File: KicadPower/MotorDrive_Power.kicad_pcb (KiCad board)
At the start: 6 copper layers, 91 x 71 mm, 347 parts, among them P1 PIN 2, P2 PIN 2, P3 PIN 2, P4 Connector, P5 Connector, P6 Header 20X2, P7 Connector, P8 Connector, P9 Connector, Q1 IGB110S101, Q10 IGB110S101, Q11 IGB110S101, Q12 IGB110S101, Q13 IGB110S101, Q14 IGB110S101, Q15 IGB110S101, Q16 IGB110S101, Q17 IGB110S101, Q18 IGB110S101, Q19 IGB110S101, Q2 IGB110S101, Q20 IGB110S101, Q21 IGB110S101, Q22 IGB110S101, Q23 IGB110S101, Q24 IGB110S101, Q3 IGB110S101, Q4 IGB110S101, Q5 IGB110S101, Q6 IGB110S101, Q7 IGB110S101, Q8 IGB110S101, Q9 IGB110S101, U1 TLE4972-AE35S5, U10 LDK220C-R, U11 1EDN7116UXTSA1, U12 1EDN7116UXTSA1, U13 1EDN7116UXTSA1, U14 1EDN7116UXTSA1, U15 1EDN7116UXTSA1, U16 1EDN7116UXTSA1, U17 TMP1075DGKR, U18 TMP1075DGKR, U19 TMP1075DGKR, U2 TLE4972-AE35S5, U3 TLE4972-AE35S5, U4 LDK220C-R, U5 LDK220C, U6 LDK220C, U7 LDK220C, U8 LDK220C-R, U9 LDK220C-R

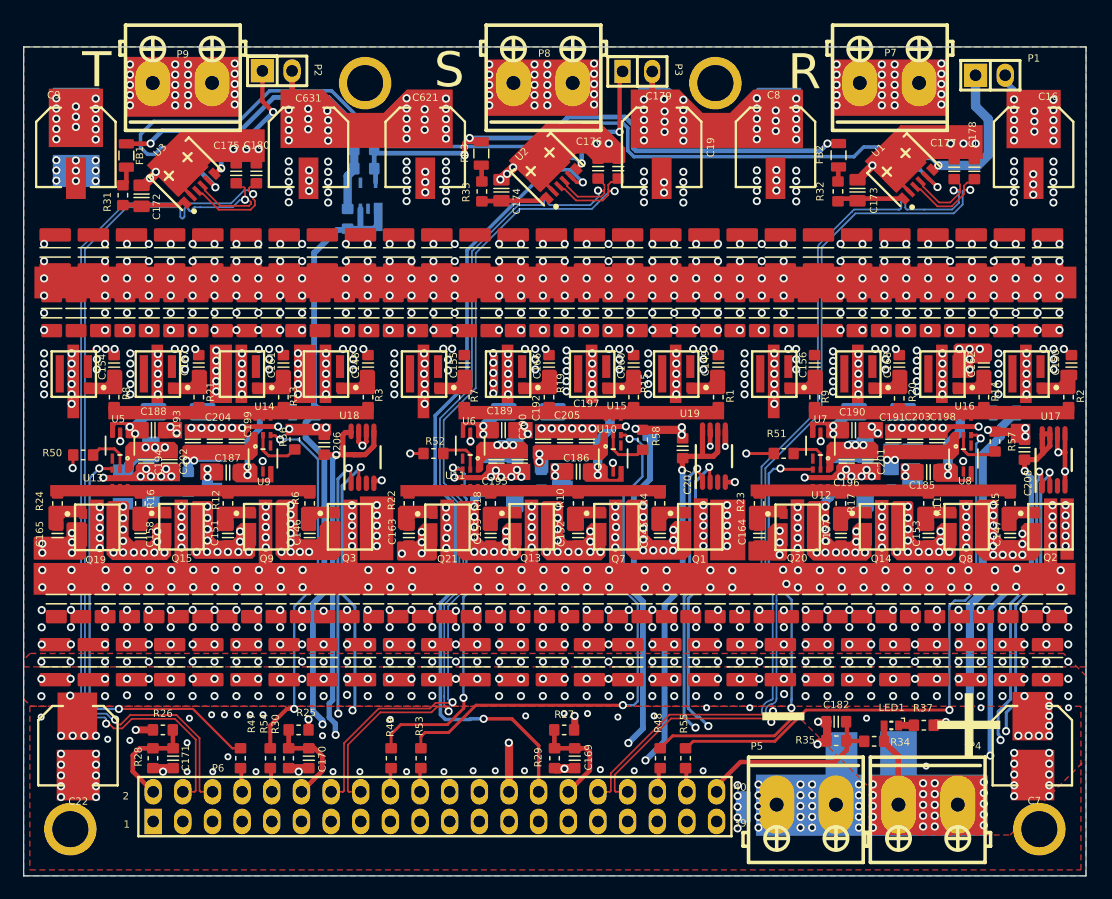
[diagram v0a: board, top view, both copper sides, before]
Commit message: new G serie of Driver modifed and finished
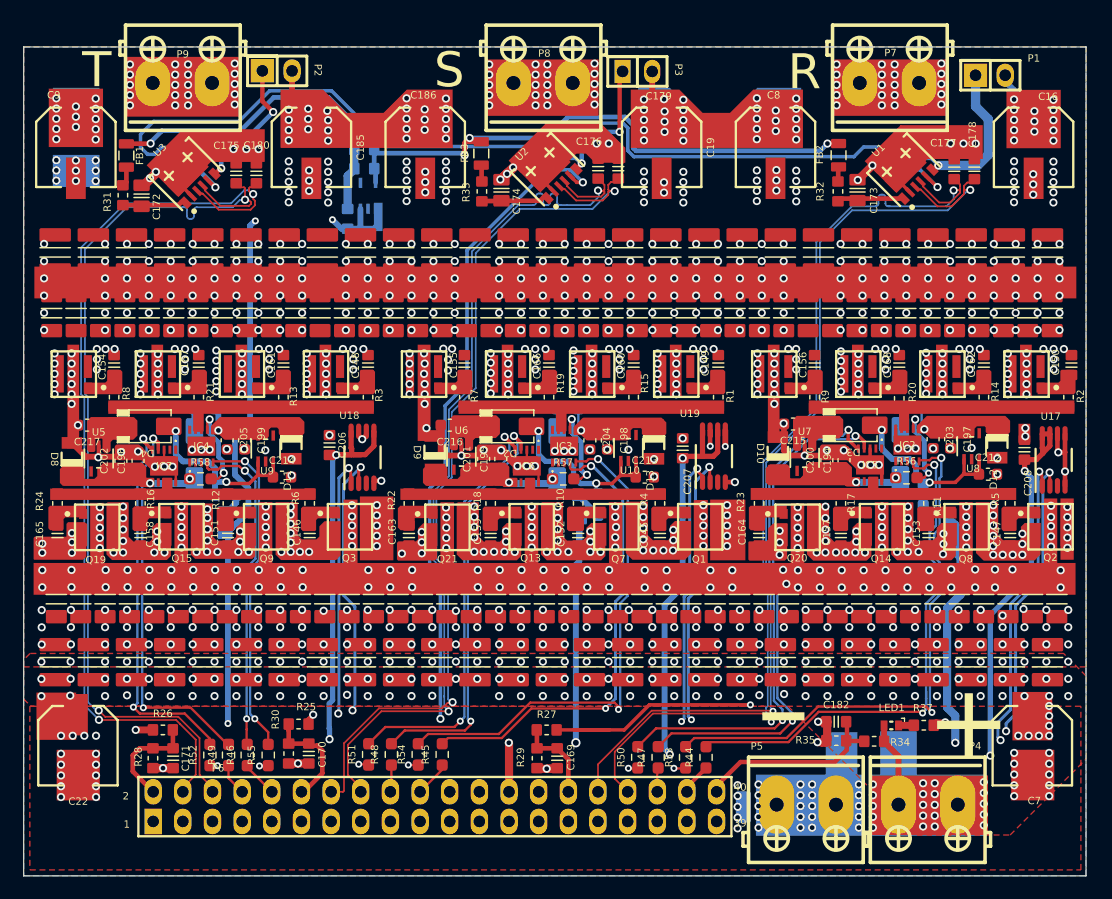
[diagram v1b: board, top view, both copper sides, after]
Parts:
- removed ? (x4): , 
- removed C187, C188, C189, C190, C191, C192, C193: Cap SMD, RezaLIB:CAPC2012X135N
- removed C621, C631: Cap Pol, RezaLIB:CAP-6.3-7.7
- removed R38, R39, R40: Res SMD, RezaLIB:RESC1608X55N
- removed U11, U12, U13, U14, U15, U16: 1EDN7116UXTSA1, RezaLIB:PG-TSNP-7-11_INF
- added C212: 10uF, Capacitor_SMD:C_0603_1608Metric, F.Cu at (185.6, 106.1)
- added C213: 10uF, Capacitor_SMD:C_0603_1608Metric, F.Cu at (156.2, 106.4)
- added C214: 10uF, Capacitor_SMD:C_0603_1608Metric, F.Cu at (125.1, 106.4)
- added C215: 10uF, Capacitor_SMD:C_0603_1608Metric, F.Cu at (168.9, 101.8)
- added C216: 10uF, Capacitor_SMD:C_0603_1608Metric, F.Cu at (139.5, 101.9)
- added C217: 10uF, Capacitor_SMD:C_0603_1608Metric, F.Cu at (108.4, 101.9)
- added IC2: 1EDN7116GXTMA1, 1EDN7116GXTMA1:1EDN7116GXTMA1, F.Cu at (178.7, 103.6)
- added IC3: 1EDN7116GXTMA1, 1EDN7116GXTMA1:1EDN7116GXTMA1, F.Cu at (149.3, 103.7)
- added IC4: 1EDN7116GXTMA1, 1EDN7116GXTMA1:1EDN7116GXTMA1, F.Cu at (118.2, 103.7)
- added IC5: 1EDN7116GXTMA1, 1EDN7116GXTMA1:1EDN7116GXTMA1, F.Cu at (175.5, 105.3)
- added IC6: 1EDN7116GXTMA1, 1EDN7116GXTMA1:1EDN7116GXTMA1, F.Cu at (146.1, 105.4)
- added IC7: 1EDN7116GXTMA1, 1EDN7116GXTMA1:1EDN7116GXTMA1, F.Cu at (115.0, 105.4)
- added R59: 10R, Resistor_SMD:R_0603_1608Metric_Pad0.98x0.95mm_HandSolder, B.Cu at (179.0, 100.4)
- added R60: 10R, Resistor_SMD:R_0603_1608Metric_Pad0.98x0.95mm_HandSolder, B.Cu at (149.6, 100.5)
- added R61: 10R, Resistor_SMD:R_0603_1608Metric_Pad0.98x0.95mm_HandSolder, B.Cu at (118.5, 100.5)
- C185, C186: value Cap SMD -> Cap Pol; footprint RezaLIB:CAPC2012X135N -> RezaLIB:CAP-6.3-7.7
- C194, C195, C196, C197, C198, C199, C200, C201, C202, C203, C204, C205: value Cap SMD -> 10uF; footprint RezaLIB:CAPC2012X135N -> Capacitor_SMD:C_0603_1608Metric
- D10, D11, D12, D13, D2, D3, D4, D8, D9: moved to F.Cu
- R41, R42, R43: value Res SMD -> 10R; footprint RezaLIB:RESC1608X55N -> Resistor_SMD:R_0603_1608Metric_Pad0.98x0.95mm_HandSolder
- R44, R45, R46: value Res SMD -> 47K; footprint RezaLIB:RESC1608X55N -> Resistor_SMD:R_0603_1608Metric_Pad0.98x0.95mm_HandSolder; moved to F.Cu
- R47, R48, R49, R50, R51, R52, R53, R54, R55: value Res SMD -> 47K; footprint RezaLIB:RESC1608X55N -> Resistor_SMD:R_0603_1608Metric_Pad0.98x0.95mm_HandSolder
- R56, R57, R58: value Res SMD -> 0R; footprint RezaLIB:RESC1608X55N -> Resistor_SMD:R_0603_1608Metric_Pad0.98x0.95mm_HandSolder
- moved R43 61.3 mm to (120.3, 107.9)
- moved C196 60.7 mm to (112.8, 105.0)
- moved R46 60.0 mm to (122.2, 130.2), turned to 90 degrees
- moved C194 59.8 mm to (173.3, 104.9)
- moved C185 59.7 mm to (127.7, 78.1), turned to -90 degrees
- moved R50 54.1 mm to (155.6, 130.4), turned to 90 degrees
- moved R56 52.5 mm to (178.6, 106.4), turned to 0 degrees
- moved R44 50.2 mm to (161.5, 130.4), turned to 90 degrees
- moved R51 43.9 mm to (132.6, 130.1), turned to 90 degrees
- moved R58 38.0 mm to (118.1, 106.5), turned to 0 degrees
- moved R57 37.1 mm to (149.2, 106.5), turned to 0 degrees
- moved R47 35.8 mm to (157.4, 130.4)
- moved R55 35.8 mm to (124.0, 130.2)
- moved C201 33.1 mm to (142.4, 104.8)
- moved R52 32.2 mm to (119.0, 130.2), turned to 90 degrees
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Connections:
- C185 pad 1: PGND -> +Vin
- C185 pad 2: Net-(U8-EN) -> PGND
- C186 pad 1: PGND -> +Vin
- C186 pad 2: Net-(U10-EN) -> PGND
- C194 pad 1: /Phase_T -> Net-(D6-2)
- C194 pad 2: Net-(D5-2) -> /Phase_R
- C195 pad 1: /Phase_S -> Net-(D7-2)
- C195 pad 2: Net-(D7-2) -> /Phase_S
- C196 pad 1: /Phase_R -> Net-(D5-2)
- C196 pad 2: Net-(D6-2) -> /Phase_T
- C197 pad 1: PGND -> Net-(IC2-VDD)
- C197 pad 2: Net-(U10-OUT) -> PGND
- C198 pad 1: PGND -> Net-(IC3-VDD)
- C198 pad 2: Net-(U16-VDD) -> PGND
- C199 pad 1: PGND -> Net-(IC4-VDD)
- C199 pad 2: Net-(U14-VDD) -> PGND
- C200 pad 1: /Phase_S -> Net-(D6-2)
- C200 pad 2: Net-(D7-2) -> /Phase_R
- C201 pad 1: /Phase_R -> Net-(D7-2)
- C201 pad 2: Net-(D6-2) -> /Phase_S
- C202 pad 1: /Phase_T -> Net-(D5-2)
- C202 pad 2: Net-(D5-2) -> /Phase_T
- C203 pad 1: PGND -> Net-(IC2-VDD)
- C203 pad 2: Net-(U16-VDD) -> PGND
- C204 pad 1: PGND -> Net-(IC3-VDD)
- C204 pad 2: Net-(U14-VDD) -> PGND
- C205 pad 1: PGND -> Net-(IC4-VDD)
- C205 pad 2: Net-(U10-OUT) -> PGND
- D11 pad 1: Net-(U14-VDD) -> Net-(IC4-VDD)
- D12 pad 1: Net-(U16-VDD) -> Net-(IC2-VDD)
- D13 pad 1: Net-(U10-OUT) -> Net-(IC3-VDD)
- R41 pad 1: Net-(U10-EN) -> Net-(FB4-Pad1)
- R41 pad 2: Net-(D2-1) -> Net-(D3-1)
- R42 pad 1: Net-(U9-EN) -> Net-(FB6-Pad1)
- R42 pad 2: Net-(D4-1) -> Net-(D2-1)
- R43 pad 1: Net-(U8-EN) -> Net-(FB5-Pad1)
- R43 pad 2: Net-(D3-1) -> Net-(D4-1)
- R44 pad 1: Net-(U14-VDD) -> /P_LS1
- R44 pad 2: Net-(D5-1) -> Net-(IC2-IN+)
- R45 pad 1: Net-(U10-OUT) -> /P_LS2
- R45 pad 2: Net-(D7-1) -> Net-(IC3-IN+)
- R46 pad 1: Net-(U16-VDD) -> /P_LS3
- R46 pad 2: Net-(D6-1) -> Net-(IC4-IN+)
- R47 pad 1: /P_HS3 -> /P_HS1
- R48 pad 1: /P_HS1 -> /P_HS2
- R49 pad 1: /P_HS2 -> /P_HS3
- R53 pad 1: /P_LS2 -> GND
- R54 pad 1: /P_LS3 -> GND
- R55 pad 1: /P_LS1 -> GND
- R56 pad 1: GND -> Net-(D6-2)
- R57 pad 1: GND -> Net-(D7-2)
- R58 pad 1: GND -> Net-(D5-2)
- U10 pad 1: Net-(U10-EN) -> Net-(D2-1)
- U10 pad 3: Net-(U10-EN) -> Net-(D2-1)
- U10 pad 5: Net-(U10-OUT) -> Net-(IC3-VDD)
- U8 pad 1: Net-(U8-EN) -> Net-(D3-1)
- U8 pad 3: Net-(U8-EN) -> Net-(D3-1)
- U8 pad 5: Net-(U16-VDD) -> Net-(IC2-VDD)
- U9 pad 1: Net-(U9-EN) -> Net-(D4-1)
- U9 pad 3: Net-(U9-EN) -> Net-(D4-1)
- U9 pad 5: Net-(U14-VDD) -> Net-(IC4-VDD)
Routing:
- net Net-(IC2-IN+): track 0.00 -> 46.1 mm, vias 0 -> 2
- net Net-(IC5-IN-): track 3.99 -> 45.5 mm, vias 0 -> 2
- net Net-(IC3-IN+): track 0.00 -> 40.3 mm, vias 0 -> 2
- net Net-(IC6-IN-): track 3.94 -> 36.4 mm, vias 0 -> 2
- net Net-(IC7-IN-): track 3.83 -> 33.0 mm, vias 0 -> 2
- net +10V: track 169.4 -> 197.2 mm, vias 4 -> 6
- net Net-(IC4-IN+): track 0.00 -> 27.8 mm, vias 0 -> 2
- net Net-(IC4-IN-): track 49.8 -> 29.3 mm
- net Net-(D2-1): track 0.00 -> 15.6 mm, vias 0 -> 2
- net Net-(D4-1): track 1.98 -> 17.1 mm, vias 0 -> 2
- net Net-(D3-1): track 0.00 -> 14.7 mm, vias 0 -> 2
- net Net-(IC3-IN-): track 31.3 -> 43.8 mm
- net /Phase_R: track 34.0 -> 46.0 mm, vias 95 -> 90
- net GND: track 62.0 -> 52.4 mm, vias 80 -> 42
- net Net-(IC5-IN+): track 36.0 -> 44.4 mm
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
